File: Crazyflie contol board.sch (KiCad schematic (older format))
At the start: 31 parts, among them P1 CONN_2, P2 CONN_2, P3 CONN_2, P4 CONN_2, Q1 PMV31XN, Q2 PMV31XN, Q3 PMV31XN, Q4 PMV31XN, SW2 BOOT, U11 ESP32-WROOM, U12 CP2102N-A01-GQFN24

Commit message: new version
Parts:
- R42: footprint SM0402 -> digikey-footprints:0603
- SW2: footprint (none) -> digikey-footprints:Switch_Tactile_SMD_B3U-1000P
- U11: footprint footprints-Lib:ESP32-WROOM-32-Espressif-Symbol-Kicad-62379 -> footprints-Lib:ESP32-WROOM-32
- U12: footprint digikey-footprints:QFN-24-1EP_3x3mm -> digikey-footprints:QFN-24-1EP_4x4mm
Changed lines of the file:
@@
 	6550 6500 6550 6850
 Wire Wire Line
-	9550 6100 9550 6750
+	9550 6050 9550 6700
 Wire Wire Line
 	8350 4700 7900 4700
@@
 	7100 3100 7450 3100
 Wire Wire Line
-	9450 6100 9450 6750
+	9450 6050 9450 6700
 Wire Wire Line
 	6550 7250 6550 7350
@@
 F 0 "R42" V 8030 1800 50  0000 C CNN
 F 1 "100R" V 7950 1800 50  0000 C CNN
-F 2 "SM0402" H 7950 1800 60  0001 C CNN
+F 2 "digikey-footprints:0603" H 7950 1800 60  0001 C CNN
 F 3 "" H 7950 1800 50  0001 C CNN
 	1    7950 1800
@@
 Text Label 7600 4800 2    60   ~ 0
 INT_GA
-Text Label 9450 6750 1    60   ~ 0
+Text Label 9450 6700 1    60   ~ 0
 I2C_SCK_VCCA
-Text Label 9550 6750 1    60   ~ 0
+Text Label 9550 6700 1    60   ~ 0
 I2C_SCL_VCCA
 $Comp
@@
 F 0 "U11" H 9275 6387 60  0000 C CNN
 F 1 "ESP32-WROOM" H 9275 6281 60  0000 C CNN
-F 2 "footprints-Lib:ESP32-WROOM-32-Espressif-Symbol-Kicad-62379" H 9650 6350 60  0001 C CNN
+F 2 "footprints-Lib:ESP32-WROOM-32" H 9650 6350 60  0001 C CNN
 F 3 "" H 8850 5450 60  0001 C CNN
 	1    9300 5000
@@
 F 0 "U12" H 10100 2828 50  0000 C CNN
 F 1 "CP2102N-A01-GQFN24" H 10100 2737 50  0000 C CNN
-F 2 "digikey-footprints:QFN-24-1EP_3x3mm" H 10550 950 50  0001 L CNN
+F 2 "digikey-footprints:QFN-24-1EP_4x4mm" H 10550 950 50  0001 L CNN
 F 3 "http://www.silabs.com/support%20documents/technicaldocs/cp2102n-datasheet.pdf" H 10150 700 50  0001 C CNN
 	1    10100 1750
@@
 F 0 "SW2" V 10704 5868 50  0000 L CNN
 F 1 "BOOT" V 10795 5868 50  0000 L CNN
-F 2 "" H 10750 5750 50  0001 C CNN
+F 2 "digikey-footprints:Switch_Tactile_SMD_B3U-1000P" H 10750 5750 50  0001 C CNN
 F 3 "" H 10750 5750 50  0001 C CNN
 	1    10750 5750
@@
 Connection ~ 6250 6500
 $Comp
-L Crazyflie-contol-board-rescue:VCCA #PWR?
+L Crazyflie-contol-board-rescue:VCCA #PWR0101
 U 1 1 5C763FAA
 P 8000 5200
-F 0 "#PWR?" H 8000 5300 30  0001 C CNN
+F 0 "#PWR0101" H 8000 5300 30  0001 C CNN
 F 1 "VCCA" H 8000 5300 30  0000 C CNN
 F 2 "" H 8000 5200 50  0001 C CNN
@@
 	8350 5800 8350 5700
 $Comp
-L Crazyflie-contol-board-rescue:AGND #PWR?
+L Crazyflie-contol-board-rescue:AGND #PWR0104
 U 1 1 5C789BE0
 P 8350 5800
-F 0 "#PWR?" H 8350 5800 40  0001 C CNN
+F 0 "#PWR0104" H 8350 5800 40  0001 C CNN
 F 1 "AGND" H 8350 5730 50  0000 C CNN
 F 2 "" H 8350 5800 50  0001 C CNN
@@
 $EndComp
 $Comp
-L Crazyflie-contol-board-rescue:VCCA #PWR?
+L Crazyflie-contol-board-rescue:VCCA #PWR0105
 U 1 1 5C7AEC62
 P 9750 850
-F 0 "#PWR?" H 9750 950 30  0001 C CNN
+F 0 "#PWR0105" H 9750 950 30  0001 C CNN
 F 1 "VCCA" H 9750 950 30  0000 C CNN
 F 2 "" H 9750 850 50  0001 C CNN
@@
 	9750 850  10000 850
 Wire Wire Line
-	10100 2750 10100 2650
-$Comp
-L Crazyflie-contol-board-rescue:AGND #PWR?
+	10200 2750 10200 2650
+$Comp
+L Crazyflie-contol-board-rescue:AGND #PWR0106
 U 1 1 5C7BAAC5
-P 10100 2750
-F 0 "#PWR?" H 10100 2750 40  0001 C CNN
-F 1 "AGND" H 10100 2680 50  0000 C CNN
-F 2 "" H 10100 2750 50  0001 C CNN
-F 3 "" H 10100 2750 50  0001 C CNN
-	1    10100 2750
-	1    0    0    -1
-$EndComp
+P 10200 2750
+F 0 "#PWR0106" H 10200 2750 40  0001 C CNN
+F 1 "AGND" H 10200 2680 50  0000 C CNN
+F 2 "" H 10200 2750 50  0001 C CNN
+F 3 "" H 10200 2750 50  0001 C CNN
+	1    10200 2750
+	1    0    0    -1
+$EndComp

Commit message: better version
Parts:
- U11: footprint footprints-Lib:ESP32-WROOM-32 -> footprints-Lib:ESP32-WROOM-32S
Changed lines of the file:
@@
 F 0 "U11" H 9275 6387 60  0000 C CNN
 F 1 "ESP32-WROOM" H 9275 6281 60  0000 C CNN
-F 2 "footprints-Lib:ESP32-WROOM-32" H 9650 6350 60  0001 C CNN
+F 2 "footprints-Lib:ESP32-WROOM-32S" H 9650 6350 60  0001 C CNN
 F 3 "" H 8850 5450 60  0001 C CNN
 	1    9300 5000

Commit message: new version
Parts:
- U12: footprint digikey-footprints:QFN-24-1EP_4x4mm -> footprints-Lib:QFN-24-1EP_4x4mm_new
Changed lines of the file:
@@
 F 0 "U12" H 10100 2828 50  0000 C CNN
 F 1 "CP2102N-A01-GQFN24" H 10100 2737 50  0000 C CNN
-F 2 "digikey-footprints:QFN-24-1EP_4x4mm" H 10550 950 50  0001 L CNN
+F 2 "footprints-Lib:QFN-24-1EP_4x4mm_new" H 10550 950 50  0001 L CNN
 F 3 "http://www.silabs.com/support%20documents/technicaldocs/cp2102n-datasheet.pdf" H 10150 700 50  0001 C CNN
 	1    10100 1750

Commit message: working version
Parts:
- SW2: footprint digikey-footprints:Switch_Tactile_SMD_B3U-1000P -> ESP32-footprints-Lib:Switch_Tactile_SMD_B3U-1000P_new_new
- U11: footprint footprints-Lib:ESP32-WROOM-32S -> ESP32-footprints-Lib:ESP32-WROOM-32_new
- U12: footprint footprints-Lib:QFN-24-1EP_4x4mm_new -> ESP32-footprints-Lib:QFN-24-1EP_4x4mm_new_new
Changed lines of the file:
@@
 F 0 "U11" H 9275 6387 60  0000 C CNN
 F 1 "ESP32-WROOM" H 9275 6281 60  0000 C CNN
-F 2 "footprints-Lib:ESP32-WROOM-32S" H 9650 6350 60  0001 C CNN
+F 2 "ESP32-footprints-Lib:ESP32-WROOM-32_new" H 9650 6350 60  0001 C CNN
 F 3 "" H 8850 5450 60  0001 C CNN
 	1    9300 5000
@@
 F 0 "U12" H 10100 2828 50  0000 C CNN
 F 1 "CP2102N-A01-GQFN24" H 10100 2737 50  0000 C CNN
-F 2 "footprints-Lib:QFN-24-1EP_4x4mm_new" H 10550 950 50  0001 L CNN
+F 2 "ESP32-footprints-Lib:QFN-24-1EP_4x4mm_new_new" H 10550 950 50  0001 L CNN
 F 3 "http://www.silabs.com/support%20documents/technicaldocs/cp2102n-datasheet.pdf" H 10150 700 50  0001 C CNN
 	1    10100 1750
@@
 F 0 "SW2" V 10704 5868 50  0000 L CNN
 F 1 "BOOT" V 10795 5868 50  0000 L CNN
-F 2 "digikey-footprints:Switch_Tactile_SMD_B3U-1000P" H 10750 5750 50  0001 C CNN
+F 2 "ESP32-footprints-Lib:Switch_Tactile_SMD_B3U-1000P_new_new" H 10750 5750 50  0001 C CNN
 F 3 "" H 10750 5750 50  0001 C CNN
 	1    10750 5750

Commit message: improved version
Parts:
- removed C7: 4.7uF, SM0603_Capa, symbol Crazyflie-contol-board-rescue:C
- removed C8: 10nF, SM0603_Capa, symbol Crazyflie-contol-board-rescue:C
- added C1, C4: 4.7uF, ESP32-footprints-Lib:0603_new_new, symbol Crazyflie-contol-board-rescue:C
- added C2, C3: 100nF, ESP32-footprints-Lib:0603_new_new, symbol Crazyflie-contol-board-rescue:C
- added R7: 1k, ESP32-footprints-Lib:0603_new_new, symbol Crazyflie-contol-board-rescue:R
- R13, R14, R5, R6: footprint SM0603 -> ESP32-footprints-Lib:0603_new_new
- U12: footprint ESP32-footprints-Lib:QFN-24-1EP_4x4mm_new_new -> ESP32-footprints-Lib:QFN-24-1EP_4x4mm_new_new_new
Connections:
- net labels added: DGND
- net labels removed: AGND
- wire segments 140 -> 155

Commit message: final versrion
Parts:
- added C5: 100nF, ESP32-footprints-Lib:0603_new_new, symbol Crazyflie-contol-board-rescue:C
- added Q7, Q8: SS8050-G, digikey-footprints:SOT-23-3, symbol Transistor_BJT:BC817
- added R10, R8, R9: 10k, ESP32-footprints-Lib:0603_new_new, symbol Crazyflie-contol-board-rescue:R
- C1: value 4.7uF -> 22uF
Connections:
- wire segments 155 -> 174
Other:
- moved on the sheet: D1, D2, D3, D4, P1, P2, P3, P4, Q1, Q2, Q3, Q4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

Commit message: version 2.0
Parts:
- C1, C2, C3, C4, C5: symbol Crazyflie-contol-board-rescue:C -> Crazyflie-contol-board-rescue:C-Crazyflie-contol-board-rescue
- D1, D2, D3, D4: symbol Crazyflie-contol-board-rescue:DIODESCH -> Crazyflie-contol-board-rescue:DIODESCH-Crazyflie-contol-board-rescue
- D5, D6: symbol Crazyflie-contol-board-rescue:LED -> Crazyflie-contol-board-rescue:LED-Crazyflie-contol-board-rescue
- P1, P2, P3, P4: symbol Crazyflie-contol-board-rescue:CONN_2 -> Crazyflie-contol-board-rescue:CONN_2-Crazyflie-contol-board-rescue
- Q1, Q2, Q3, Q4: symbol Crazyflie-contol-board-rescue:MOSFET_N -> Crazyflie-contol-board-rescue:MOSFET_N-Crazyflie-contol-board-rescue
- Q7, Q8: symbol Transistor_BJT:BC817 -> Crazyflie-contol-board-rescue:BC817-Transistor_BJT
- R1, R10, R13, R14, R2, R3, R39, R4, R40, R41, R42, R5, R6, R7, R8, R9: symbol Crazyflie-contol-board-rescue:R -> Crazyflie-contol-board-rescue:R-Crazyflie-contol-board-rescue
- SW2: symbol Crazyflie-contol-board-rescue:SW_PUSH -> Crazyflie-contol-board-rescue:SW_PUSH-Crazyflie-contol-board-rescue
- U11: symbol ESP32-footprints-Shem-Lib:ESP32-WROOM -> Crazyflie-contol-board-rescue:ESP32-WROOM-ESP32-footprints-Shem-Lib
- U12: symbol Interface_USB:CP2102N-A01-GQFN24 -> Crazyflie-contol-board-rescue:CP2102N-A01-GQFN24-Interface_USB
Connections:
- net labels added: USBD+, USBD-
- net labels removed: LED_GREEN, LED_RED, TCK, TDI, TMS, W_CE, W_CK, W_INT
- wire segments 174 -> 162
- no-connect marks 2 -> 0
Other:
- moved on the sheet: C3, C4, C5, D5, D6, Q7, R5, R6, R7, R8, R9, SW2

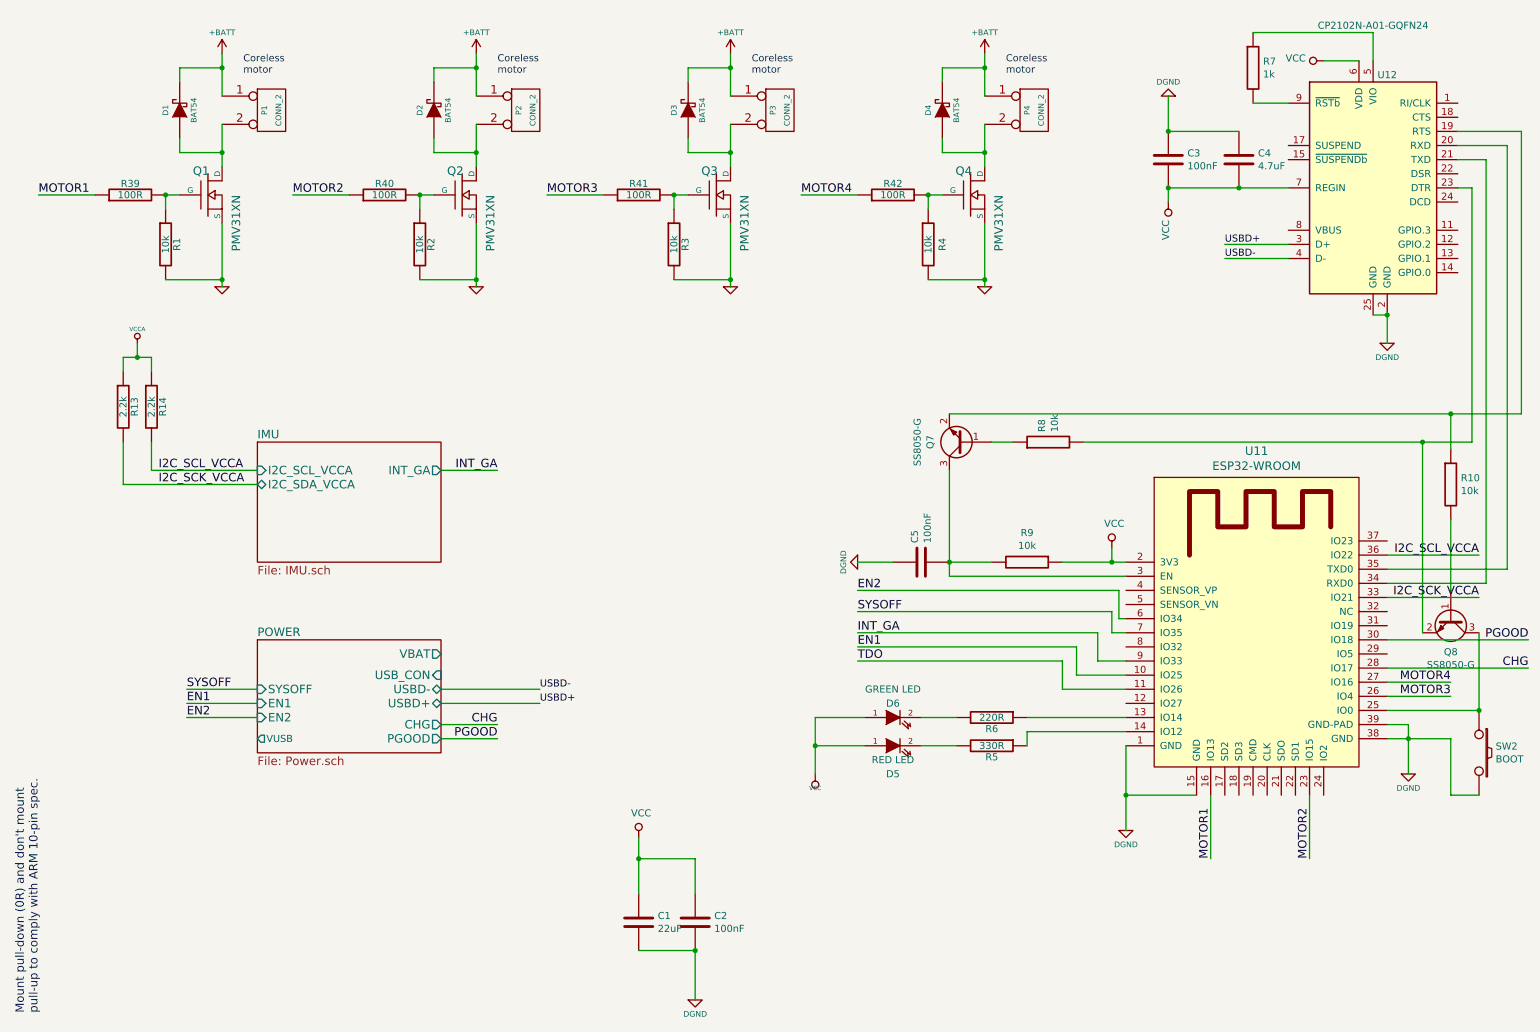
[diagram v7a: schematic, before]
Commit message: checked: esp32 pins (issue #2)
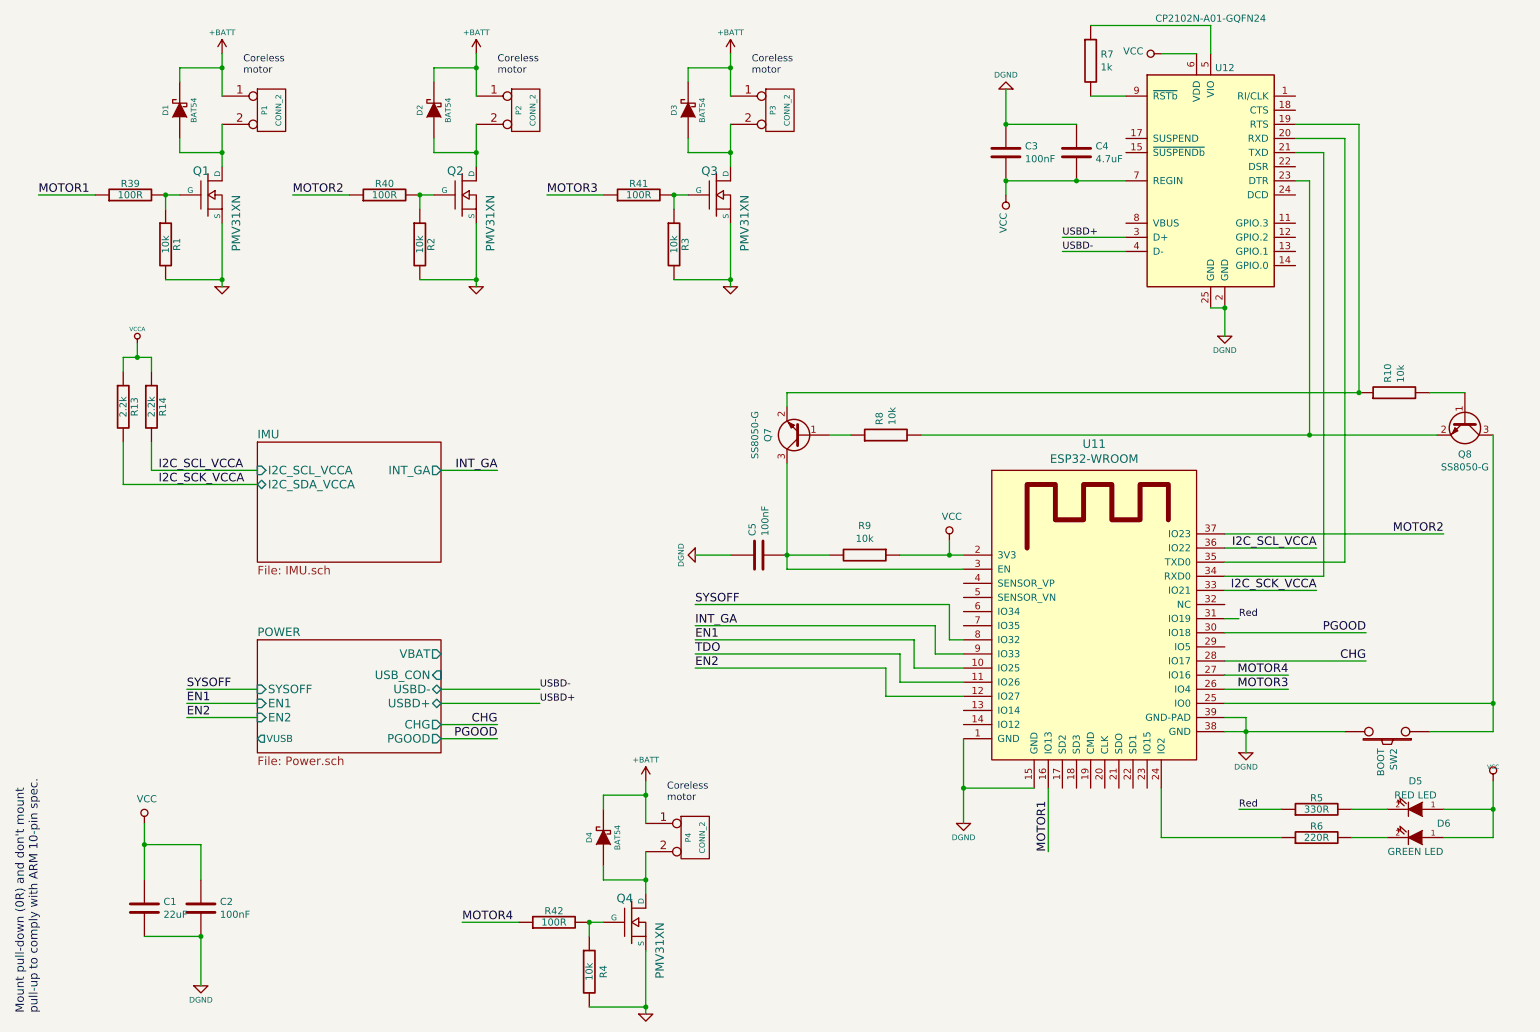
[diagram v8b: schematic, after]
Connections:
- net EN2: now also U11.12 (IO27); no longer U11.6 (IO34)
- net MOTOR2: now also U11.37 (IO23); no longer U11.23 (IO15)
- net SYSOFF: now also U11.8 (IO32); no longer U11.7 (IO35)
- net at R6.1: now also U11.24 (IO2); no longer U11.13 (IO14)
- net at U11.14 (IO12): no longer R5.1
- net Red: now reaches U11.31 (IO19)
- net Red: now also R5.1
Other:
- moved on the sheet: C1, C2, C3, C4, C5, D4, D5, D6, P4, Q4, Q7, Q8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
